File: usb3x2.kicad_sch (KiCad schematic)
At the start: 43 parts

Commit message: Schematic design for usb
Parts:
- removed C? (x14): C_100n_0402, antmicro-footprints:0402-cap, symbol antmicroCapacitors0402:C_100n_0402
- removed C? (x2): C_18p_0402, antmicro-footprints:0402-cap, symbol antmicroCapacitors0402:C_18p_0402
- removed C? (x2): C_10u_0603, antmicro-footprints:0603-cap, symbol antmicroCapacitors0603:C_10u_0603
- removed D? (x2): LG_L29K-G2J1-24-Z, antmicro-footprints:LED_0603, symbol antmicroLEDIndicationDiscrete:LG_L29K-G2J1-24-Z
- removed FB? (x3): BLM18PG330SH1D, antmicro-footprints:0603-res, symbol antmicroFerriteBeadsandChips:BLM18PG330SH1D
- removed R? (x5): R_0R_0402, antmicro-footprints:0402-res, symbol antmicroResistors0402:R_0R_0402
- removed R? (x2): R_1k_0402, antmicro-footprints:0402-res, symbol antmicroResistors0402:R_1k_0402
- removed R? (x2): R_100k_0402, antmicro-footprints:0402-res, symbol antmicroResistors0402:R_100k_0402
- removed R?: R_12k_0402, antmicro-footprints:0402-res, symbol antmicroResistors0402:R_12k_0402
- removed R? (x4): R_10k_0402, antmicro-footprints:0402-res, symbol antmicroResistors0402:R_10k_0402
- removed R? (x2): R_15k_0402, antmicro-footprints:0402-res, symbol antmicroResistors0402:R_15k_0402
- removed R?: R_2k_0402, antmicro-footprints:0402-res, symbol antmicroResistors0402:R_2k_0402
- removed U?: 93LC66BT-IMC, antmicro-footprints:DFN-8_2x3mm, symbol antmicroMemory:93LC66BT-IMC
- removed U?: FT4233HPQ, antmicro-footprints:QFN-76-1EP_9x9mm_P0.4mm_EP3.8x3.8mm, symbol antmicroInterfaceControllers:FT4233HPQ
- removed Y?: ABM8G-12.000MHZ-18-D2Y-T, antmicro-footprints:KX-7, symbol antmicroCrystals:ABM8G-12.000MHZ-18-D2Y-T
- added C? (x12): C_100n_0402, antmicro-footprints:0402-cap, symbol antmicroCapacitors0402:C_100n_0402
- added C? (x2): C_10u_0603, antmicro-footprints:0603-cap, symbol antmicroCapacitors0603:C_10u_0603
- added IC? (x2): HD3SS3220, antmicro-footprints:RNH0030A, symbol antmicroInterfaceControllers:HD3SS3220
- added J? (x2): WE_632723300011_alt_symbol, antmicro-footprints:WE_632723300011, symbol antmicroUSBDVIHDMIConnectors:WE_632723300011_alt_symbol
- added R? (x28): R_0R_0402, antmicro-footprints:0402-res, symbol antmicroResistors0402:R_0R_0402
- added R? (x2): R_200k_0402, antmicro-footprints:0402-res, symbol antmicroResistors0402:R_200k_0402
- added R? (x8): R_10k_0402, antmicro-footprints:0402-res, symbol antmicroResistors0402:R_10k_0402
- added TP? (x4): TP_SMD_0_75MM, antmicro-footprints:Testpoint_smd_0_75mm, symbol antmicroTestPoints:TP_SMD_0_75MM
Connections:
- net +3V3: now also C?.1, C?.1, IC?.8 (VCC33), IC?.8 (VCC33), R?.2, R?.2, R?.2, R?.2, R?.2, R?.2
- net GND: now also C?.2, C?.2, C?.2, C?.2, C?.2, C?.2, IC?.13 (GND), IC?.13 (GND), IC?.28 (GND), IC?.28 (GND), IC?.31 (GND), IC?.31 (GND), J?.A1 (GND), J?.A1 (GND), J?.A12 (GND), J?.A12 (GND), J?.B1 (GND), J?.B1 (GND), J?.B12 (GND), J?.B12 (GND), J?.Shell (SHIELD), J?.Shell (SHIELD), R?.1, R?.1, R?.1, R?.1, R?.1, R?.1
- net USB_SCL: now also IC?.26 (SCL/OUT2), IC?.26 (SCL/OUT2)
- net USB_SDA: now also IC?.25 (SDA/OUT1), IC?.25 (SDA/OUT1)
- new net: IC?.22 (ADDR), R?.1, R?.2 (x2)
- new net: C?.1, IC?.20 (TX2n) (x2)
- new net: C?.2, J?.B3 (TX2-) (x2)
- new net: J?.A6 (D+), J?.B6 (D+), R?.2 (x2)
- new net: C?.1, IC?.21 (TX2p) (x2)
- new net: C?.2, J?.B2 (TX2+) (x2)
- new net: IC?.29 (ENn_CC), R?.2 (x2)
- new net: IC?.11 (DIR), R?.1 (x2)
- new net: J?.A7 (D-), J?.B7 (D-), R?.2 (x2)
- new net: IC?.12 (ENn_MUX), R?.2 (x2)
- new net: IC?.10 (RXn), R?.2 (x2)
- new net: IC?.24 (VCONN_FAULT_N), R?.1, TP?.1 (x2)
- new net: IC?.1 (CC2), J?.B5 (CC2) (x2)
- new net: IC?.14 (RX1n), R?.1 (x2)
- new net: IC?.15 (RX1p), R?.1 (x2)
- new net: C?.1, IC?.16 (TX1n) (x2)
- new net: C?.1, IC?.17 (TX1p) (x2)
- new net: IC?.18 (RX2n), R?.1 (x2)
- new net: IC?.19 (RX2p), R?.1 (x2)
- new net: IC?.2 (CC1), J?.A5 (CC1) (x2)
- new net: IC?.27 (ID), R?.1, TP?.1 (x2)
- new net: IC?.3 (CURRENT_MODE), R?.1 (x2)
- new net: IC?.4 (PORT), R?.2 (x2)
- new net: IC?.5 (VBUS_DET), J?.A4 (VBUS), J?.A9 (VBUS), J?.B4 (VBUS), J?.B9 (VBUS) (x2)
- new net: IC?.6 (TXp), R?.2 (x2)
- new net: IC?.7 (TXn), R?.2 (x2)
- new net: IC?.9 (RXp), R?.2 (x2)
- new net: J?.A10 (RX2-), R?.2 (x2)
- new net: J?.A11 (RX2+), R?.2 (x2)
- new net: C?.2, J?.A2 (TX1+) (x2)
- new net: C?.2, J?.A3 (TX1-) (x2)
- new net: J?.B10 (RX1-), R?.2 (x2)
- new net: J?.B11 (RX1+), R?.2 (x2)
- new net +5V: C?.1, C?.1, C?.1, C?.1, IC?.30 (VDD5), IC?.30 (VDD5), R?.1, R?.1, R?.2, R?.2, R?.2, R?.2
- new net USB1_D_N: R?.1
- new net USB1_D_P: R?.1
- new net USB3_D_N: R?.1
- new net USB3_D_P: R?.1
- new net USBSS1_RX_N: R?.1
- new net USBSS1_RX_P: R?.1
- new net USBSS1_TX_N: R?.1
- new net USBSS1_TX_P: R?.1
- new net USBSS2_RX_N: R?.1
- new net USBSS2_RX_P: R?.1
- new net USBSS2_TX_N: R?.1
- new net USBSS2_TX_P: R?.1
- no-connect marks 33 -> 4
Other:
- note added: "10k - 3A 500k - 1.5A DNP - 900mA"
- note added: "3A Limit Switch needed"
- note added: "Both DNP - GPIO Mode HIGH - I2C Mode 0x67 LOW - I2C Mode 0x47"
- note added: "Enable CC controller"
- note added: "Enable MUX"
- note added: "LOW: is sourcing HIGH: not sourcing"
- note added: "LOW: vconn over-current tripped HIGH: ok"
- note added: "Source Mode"
- note added: "USB-C 1"
- note added: "USB-C 2"
- note removed: "Config memory"
- note removed: "ORG: HIGH-x16 LOW-x8"
- note removed: "Orin Debug Interface"
- note removed: "PD1 Voltage sensing"
- note removed: "PD2 Voltage Sensing"
- note removed: "Power configuration for PD"
- note removed: "USB2 Orientation detection: high-CC1, low-CC2"

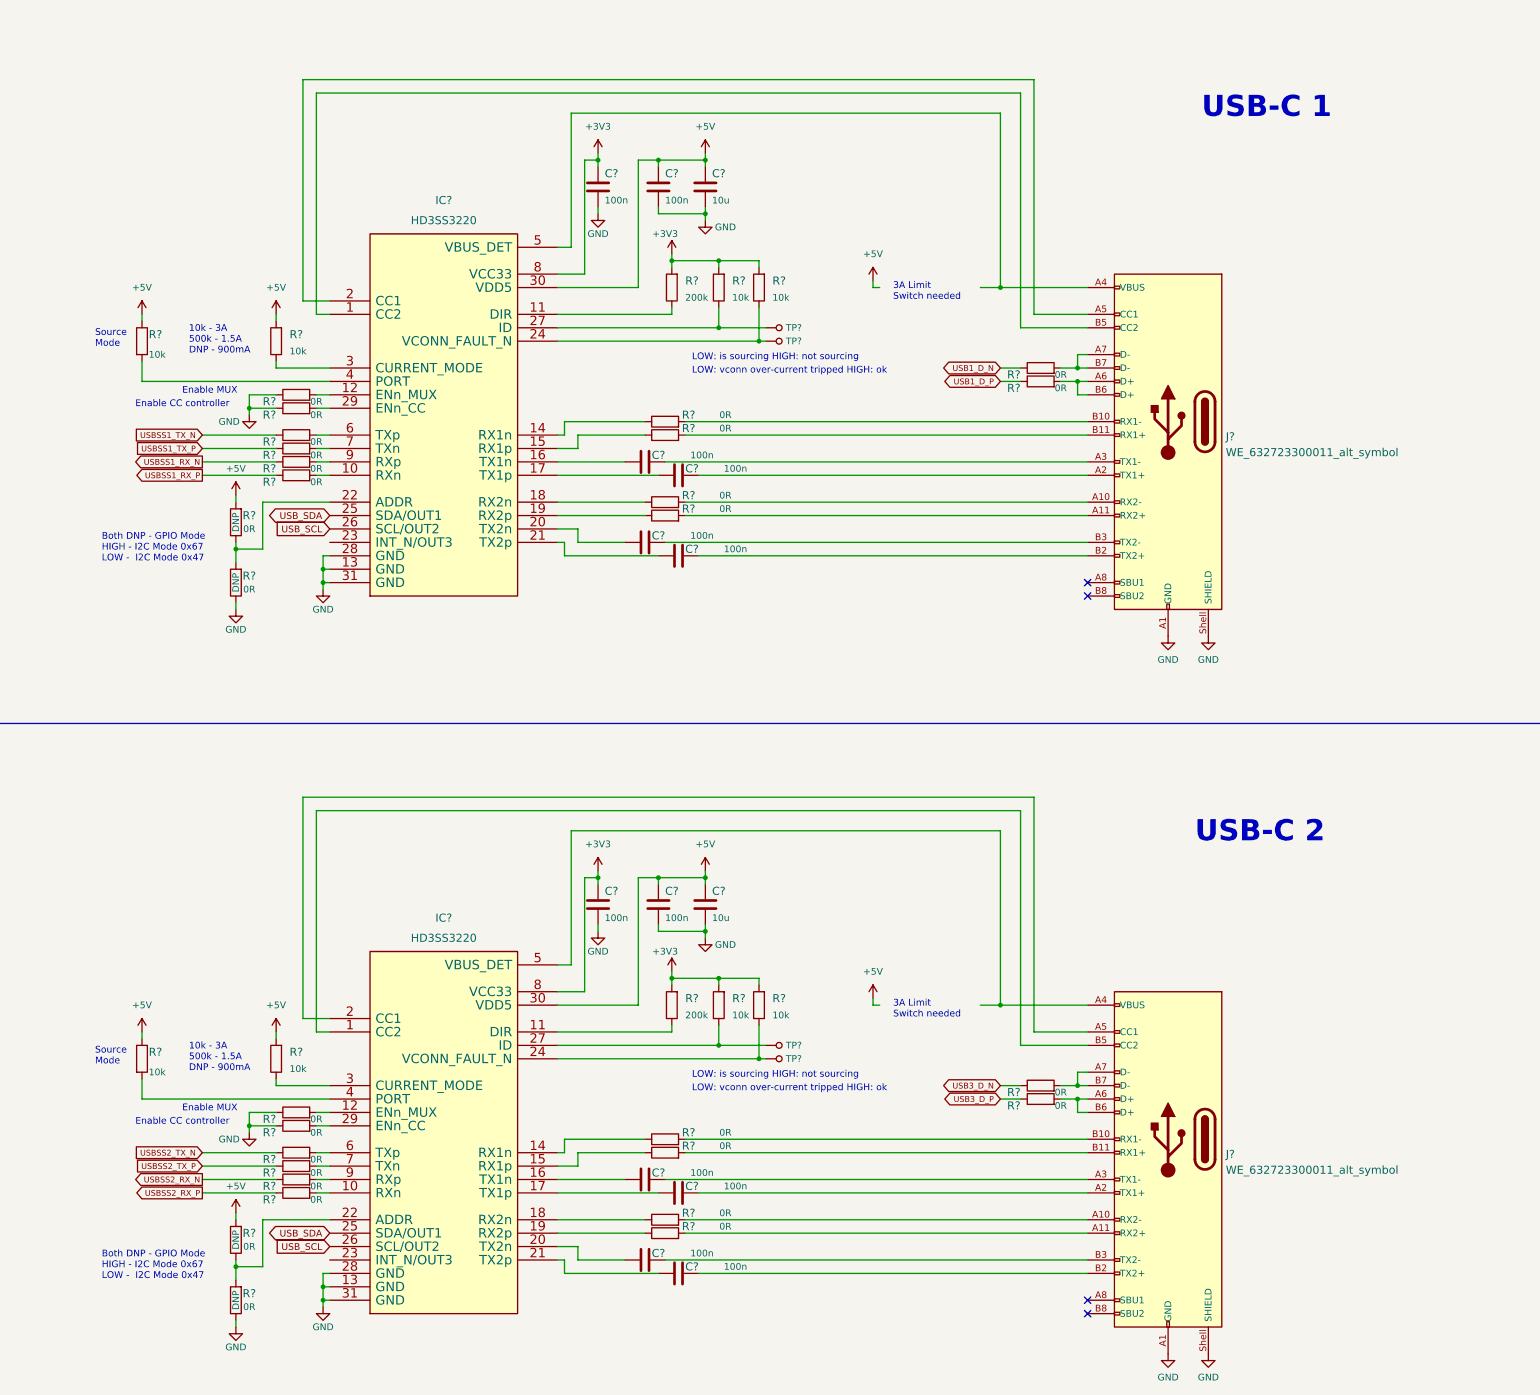
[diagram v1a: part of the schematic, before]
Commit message: Improwed usb3x2 schematic, added usb power switch
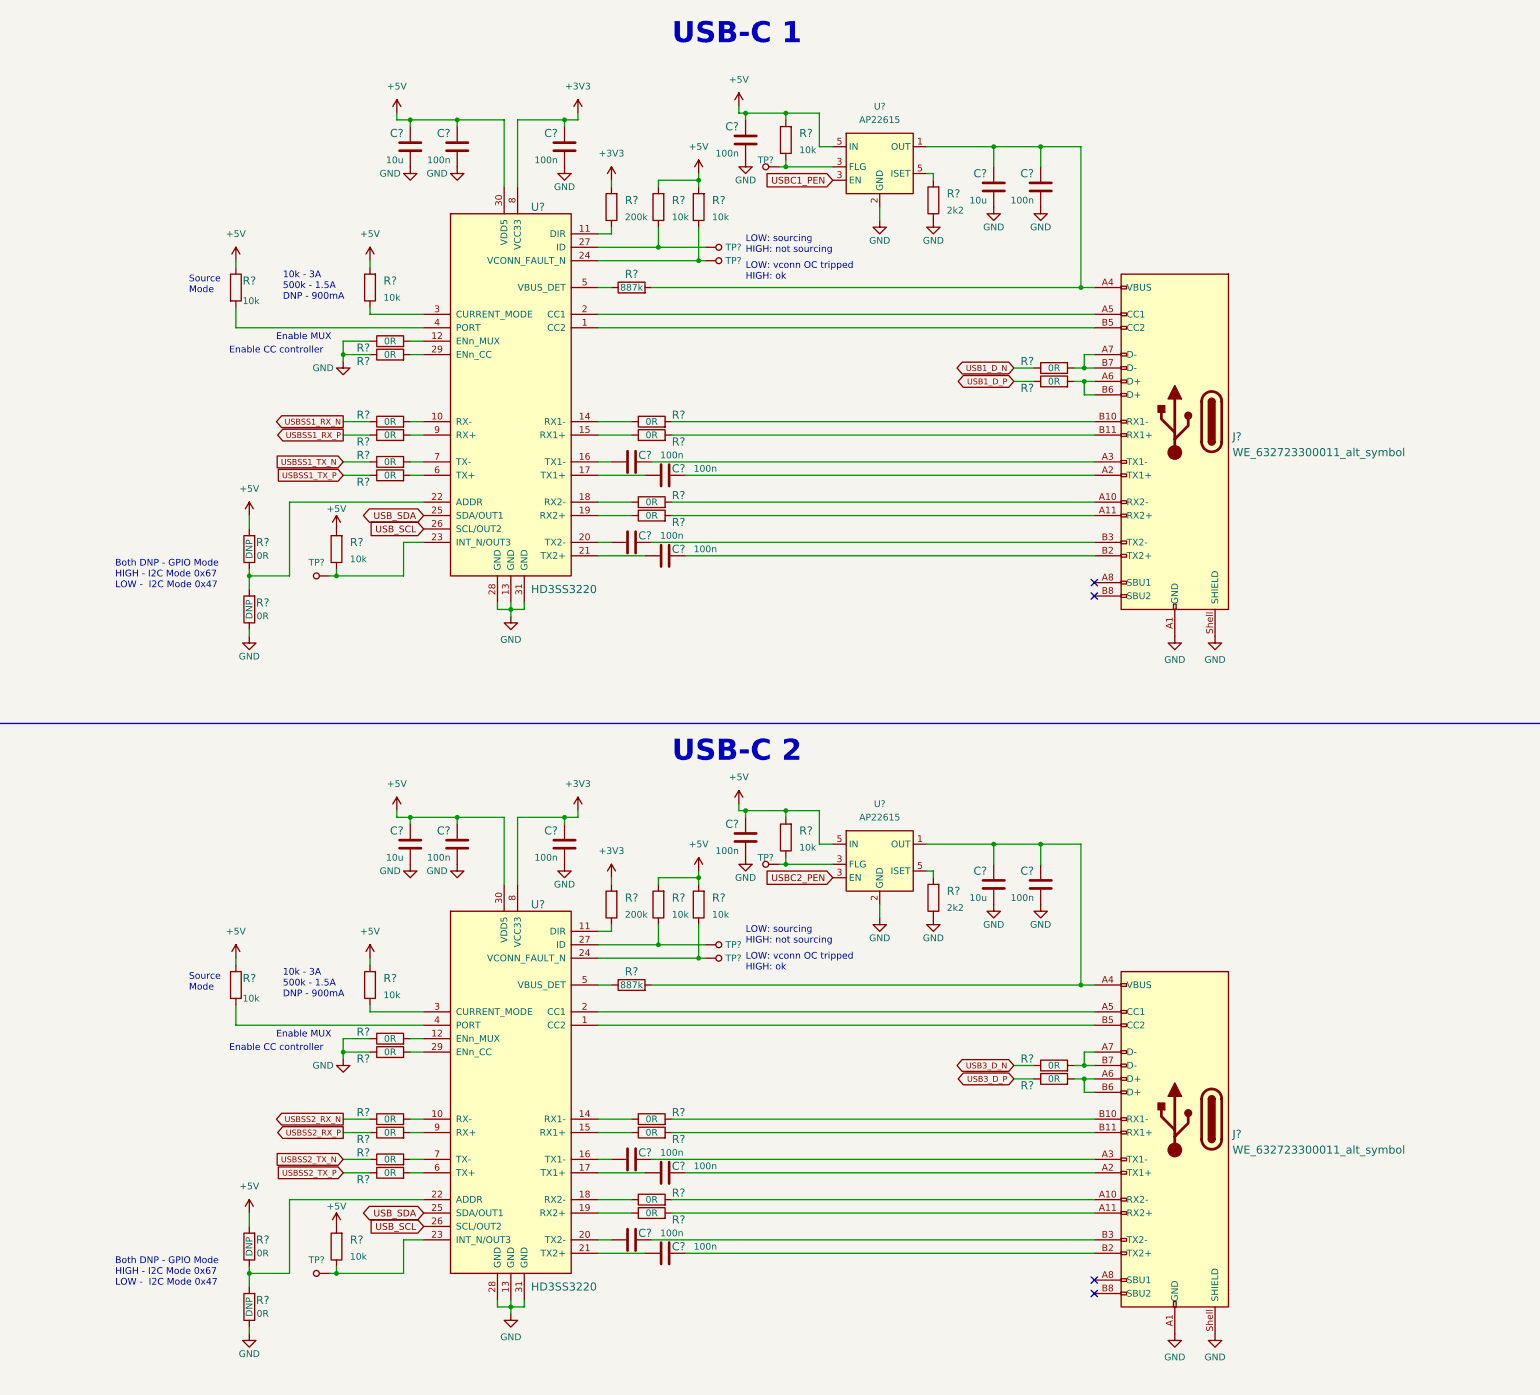
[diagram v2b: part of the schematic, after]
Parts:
- removed C? (x8): C_100n_0402, antmicro-footprints:0402-cap, symbol antmicroCapacitors0402:C_100n_0402
- removed C? (x2): C_10u_0603, antmicro-footprints:0603-cap, symbol antmicroCapacitors0603:C_10u_0603
- removed IC? (x2): HD3SS3220, antmicro-footprints:RNH0030A, symbol antmicroInterfaceControllers:HD3SS3220
- removed R? (x22): R_0R_0402, antmicro-footprints:0402-res, symbol antmicroResistors0402:R_0R_0402
- removed R? (x2): R_200k_0402, antmicro-footprints:0402-res, symbol antmicroResistors0402:R_200k_0402
- removed R? (x8): R_10k_0402, antmicro-footprints:0402-res, symbol antmicroResistors0402:R_10k_0402
- removed TP? (x4): TP_SMD_0_75MM, antmicro-footprints:Testpoint_smd_0_75mm, symbol antmicroTestPoints:TP_SMD_0_75MM
- added C? (x12): C_100n_0402, antmicro-footprints:0402-cap, symbol antmicroCapacitors0402:C_100n_0402
- added C? (x4): C_10u_0603, antmicro-footprints:0603-cap, symbol antmicroCapacitors0603:C_10u_0603
- added R? (x22): R_0R_0402, antmicro-footprints:0402-res, symbol antmicroResistors0402:R_0R_0402
- added R? (x12): R_10k_0402, antmicro-footprints:0402-res, symbol antmicroResistors0402:R_10k_0402
- added R? (x2): R_887k_0402, antmicro-footprints:0402-res, symbol antmicroResistors0402:R_887k_0402
- added R? (x2): R_2k2_0402, antmicro-footprints:0402-res, symbol antmicroResistors0402:R_2k2_0402
- added R? (x2): R_200k_0402, antmicro-footprints:0402-res, symbol antmicroResistors0402:R_200k_0402
- added TP? (x8): TP_SMD_0_75MM, antmicro-footprints:Testpoint_smd_0_75mm, symbol antmicroTestPoints:TP_SMD_0_75MM
- added U? (x2): AP22615, antmicro-footprints:TSOT23-6, symbol antmicroPMICPowerDistributionSwitchesLoadDrivers:AP22615
- added U? (x2): HD3SS3220, antmicro-footprints:RNH0030A, symbol antmicroInterfaceControllers:HD3SS3220
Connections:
- net +3V3: now also C?.1, C?.1, R?.2, R?.2, U?.8 (VCC33), U?.8 (VCC33)
- net +5V: now also C?.1, C?.1, C?.1, C?.1, C?.1, C?.1, R?.1, R?.1, R?.2, R?.2, R?.2, R?.2, R?.2, R?.2, R?.2, R?.2, R?.2, R?.2, R?.2, R?.2, U?.30 (VDD5), U?.30 (VDD5), U?.5 (ISET), U?.5 (ISET)
- net GND: now also C?.2, C?.2, C?.2, C?.2, C?.2, C?.2, C?.2, C?.2, C?.2, C?.2, C?.2, C?.2, R?.1, R?.1, R?.1, R?.1, R?.1, R?.1, R?.1, R?.1, U?.13 (GND), U?.13 (GND), U?.2 (GND), U?.2 (GND), U?.28 (GND), U?.28 (GND), U?.31 (GND), U?.31 (GND)
- net USB1_D_N: now also R?.1
- net USB1_D_P: now also R?.1
- net USBSS1_RX_N: now also R?.1
- net USBSS1_RX_P: now also R?.1
- net USBSS1_TX_N: now also R?.1
- net USBSS1_TX_P: now also R?.1
- net USBSS2_RX_N: now also R?.1
- net USBSS2_RX_P: now also R?.1
- net USBSS2_TX_N: now also R?.1
- net USBSS2_TX_P: now also R?.1
- net USB_SCL: now also U?.26 (SCL/OUT2), U?.26 (SCL/OUT2)
- net USB_SDA: now also U?.25 (SDA/OUT1), U?.25 (SDA/OUT1)
- net at J?.B3 (TX2-): now also C?.2
- net at J?.A6 (D+), J?.B6 (D+): now also R?.2
- net at C?.1: now also U?.21 (TX2+)
- net at J?.B5 (CC2): now also U?.1 (CC2) (x2)
- net at J?.A5 (CC1): now also U?.2 (CC1) (x2)
- net at J?.A4 (VBUS), J?.A9 (VBUS), J?.B4 (VBUS)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: now also C?.1, C?.1, R?.2, U?.1 (OUT) (x2)
- net at J?.A10 (RX2-): now also R?.2
- net at J?.A11 (RX2+): now also R?.2
- net at J?.A2 (TX1+): now also C?.2
- net at J?.A3 (TX1-): now also C?.2
- net at J?.A7 (D-), J?.B7 (D-): now also R?.2
- net at J?.B10 (RX1-): now also R?.2
- net at J?.B11 (RX1+): now also R?.2
- net at J?.B2 (TX2+): now also C?.2
- net at C?.1: now also U?.17 (TX1+)
- net at R?.1: now also U?.18 (RX2-)
- net at R?.1: now also U?.15 (RX1+)
- net at C?.1: now also U?.20 (TX2-)
- net at R?.1: now also U?.14 (RX1-)
- net at C?.1: now also U?.16 (TX1-)
- net at R?.1: now also U?.19 (RX2+)
- new net: R?.2, U?.9 (RX+) (x2)
- new net: R?.1, TP?.1, U?.24 (VCONN_FAULT_N) (x2)
- new net: R?.1, TP?.1, U?.23 (INT_N/OUT3) (x2)
- new net: R?.1, U?.5 (VBUS_DET) (x2)
- new net: R?.2, U?.4 (PORT) (x2)
- new net: R?.2, U?.29 (ENn_CC) (x2)
- new net: R?.1, TP?.1, U?.3 (FLG) (x2)
- new net: R?.2, U?.5 (ISET) (x2)
- new net: R?.2, U?.7 (TX-) (x2)
- new net: R?.2, U?.10 (RX-) (x2)
- new net: R?.1, U?.11 (DIR) (x2)
- new net: R?.2, U?.12 (ENn_MUX) (x2)
- new net: R?.1, U?.14 (RX1-)
- new net: R?.1, U?.15 (RX1+)
- new net: C?.1, U?.16 (TX1-)
- new net: C?.1, U?.17 (TX1+)
- new net: R?.1, U?.18 (RX2-)
- new net: R?.1, U?.19 (RX2+)
- new net: C?.1, U?.20 (TX2-)
- new net: C?.1, U?.21 (TX2+)
- new net: R?.1, R?.2, U?.22 (ADDR) (x2)
- new net: R?.1, TP?.1, U?.27 (ID) (x2)
- new net: R?.1, U?.3 (CURRENT_MODE) (x2)
- new net: R?.2, U?.6 (TX+) (x2)
- new net USBC1_PEN: U?.3 (FLG)
- new net USBC2_PEN: U?.3 (FLG)
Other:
- note added: "LOW: sourcing HIGH: not sourcing"
- note added: "LOW: vconn OC tripped HIGH: ok"
- note removed: "3A Limit Switch needed"
- note removed: "LOW: is sourcing HIGH: not sourcing"
- note removed: "LOW: vconn over-current tripped HIGH: ok"
- moved on the sheet: C?, J?, R?
